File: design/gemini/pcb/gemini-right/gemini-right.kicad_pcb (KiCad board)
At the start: 2 copper layers, 123.8 x 84.2 mm, 47 parts, among them J1 USB-C link, SW00 Y, SW01 U, SW02 I, SW03 O, SW04 P, SW05 Bksp, SW10 H, SW11 J, SW12 K, SW13 L, SW14 ;, SW15 Enter, SW20 N, SW21 M, SW22 ,, SW23 ., SW24 Shift, SW30 Space, SW31 Fn, SW32 Alt, SW33 Ctrl, U1 MCP23017-E/SO

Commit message: add LEDs
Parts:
- added C2: 1uF, C_0603_1608Metric, B.Cu at (24.0, -4.00)
- added C3: 1uF, C_0603_1608Metric, B.Cu at (36.0, -4.00)
- added LED00: SK6812MINI-E, LED_SK6812MINI-E_3.2x2.8mm_P1.5mm_ReverseMount, B.Cu at (9.53, 14.6)
- added LED01: SK6812MINI-E, LED_SK6812MINI-E_3.2x2.8mm_P1.5mm_ReverseMount, B.Cu at (28.6, 14.6)
- added LED02: SK6812MINI-E, LED_SK6812MINI-E_3.2x2.8mm_P1.5mm_ReverseMount, B.Cu at (47.6, 14.6)
- added LED03: SK6812MINI-E, LED_SK6812MINI-E_3.2x2.8mm_P1.5mm_ReverseMount, B.Cu at (66.7, 14.6)
- added LED04: SK6812MINI-E, LED_SK6812MINI-E_3.2x2.8mm_P1.5mm_ReverseMount, B.Cu at (85.7, 14.6)
- added LED05: SK6812MINI-E, LED_SK6812MINI-E_3.2x2.8mm_P1.5mm_ReverseMount, B.Cu at (109.5, 14.6)
- added LED10: SK6812MINI-E, LED_SK6812MINI-E_3.2x2.8mm_P1.5mm_ReverseMount, B.Cu at (14.3, 33.7)
- added LED11: SK6812MINI-E, LED_SK6812MINI-E_3.2x2.8mm_P1.5mm_ReverseMount, B.Cu at (33.3, 33.7)
- added LED12: SK6812MINI-E, LED_SK6812MINI-E_3.2x2.8mm_P1.5mm_ReverseMount, B.Cu at (52.4, 33.7)
- added LED13: SK6812MINI-E, LED_SK6812MINI-E_3.2x2.8mm_P1.5mm_ReverseMount, B.Cu at (71.4, 33.7)
- added LED14: SK6812MINI-E, LED_SK6812MINI-E_3.2x2.8mm_P1.5mm_ReverseMount, B.Cu at (90.5, 33.7)
- added LED15: SK6812MINI-E, LED_SK6812MINI-E_3.2x2.8mm_P1.5mm_ReverseMount, B.Cu at (111.9, 33.7)
- added LED20: SK6812MINI-E, LED_SK6812MINI-E_3.2x2.8mm_P1.5mm_ReverseMount, B.Cu at (19.1, 52.7)
- added LED21: SK6812MINI-E, LED_SK6812MINI-E_3.2x2.8mm_P1.5mm_ReverseMount, B.Cu at (38.1, 52.7)
- added LED22: SK6812MINI-E, LED_SK6812MINI-E_3.2x2.8mm_P1.5mm_ReverseMount, B.Cu at (57.1, 52.7)
- added LED23: SK6812MINI-E, LED_SK6812MINI-E_3.2x2.8mm_P1.5mm_ReverseMount, B.Cu at (76.2, 52.7)
- added LED24: SK6812MINI-E, LED_SK6812MINI-E_3.2x2.8mm_P1.5mm_ReverseMount, B.Cu at (104.8, 52.7)
- added LED30: SK6812MINI-E, LED_SK6812MINI-E_3.2x2.8mm_P1.5mm_ReverseMount, B.Cu at (26.2, 71.8)
- added LED31: SK6812MINI-E, LED_SK6812MINI-E_3.2x2.8mm_P1.5mm_ReverseMount, B.Cu at (64.3, 71.8)
- added LED32: SK6812MINI-E, LED_SK6812MINI-E_3.2x2.8mm_P1.5mm_ReverseMount, B.Cu at (88.1, 71.8)
- added LED33: SK6812MINI-E, LED_SK6812MINI-E_3.2x2.8mm_P1.5mm_ReverseMount, B.Cu at (111.9, 71.8)
- added U2: MCP1700-3302, SOT-23, B.Cu at (30.0, -4.00)
- moved D10 0.60 mm to (10.3, 36.6)
- moved D11 0.60 mm to (29.3, 36.6)
- moved D12 0.60 mm to (48.4, 36.6)
- moved D13 0.60 mm to (67.4, 36.6)
- moved D14 0.60 mm to (86.5, 36.6)
- moved D15 0.60 mm to (107.9, 36.6)
- moved D20 0.60 mm to (15.1, 55.6)
- moved D21 0.60 mm to (34.1, 55.6)
- moved D22 0.60 mm to (53.1, 55.6)
- moved D23 0.60 mm to (72.2, 55.6)
- moved D24 0.60 mm to (100.8, 55.6)
- moved D00 0.60 mm to (5.53, 17.5)
- moved D01 0.60 mm to (24.6, 17.5)
- moved D02 0.60 mm to (43.6, 17.5)
- moved D03 0.60 mm to (62.7, 17.5)
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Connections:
- J1 pad 10: (no net) -> LED_LINK
- J1 pad 11: +3V3 -> +5V
- J1 pad 2: +3V3 -> +5V
- J1 pad 3: (no net) -> LED_LINK
- J1 pad 4: (no net) -> LED_LINK
- J1 pad 9: (no net) -> LED_LINK

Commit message: add usb c
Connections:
- net +5V renamed VSYS

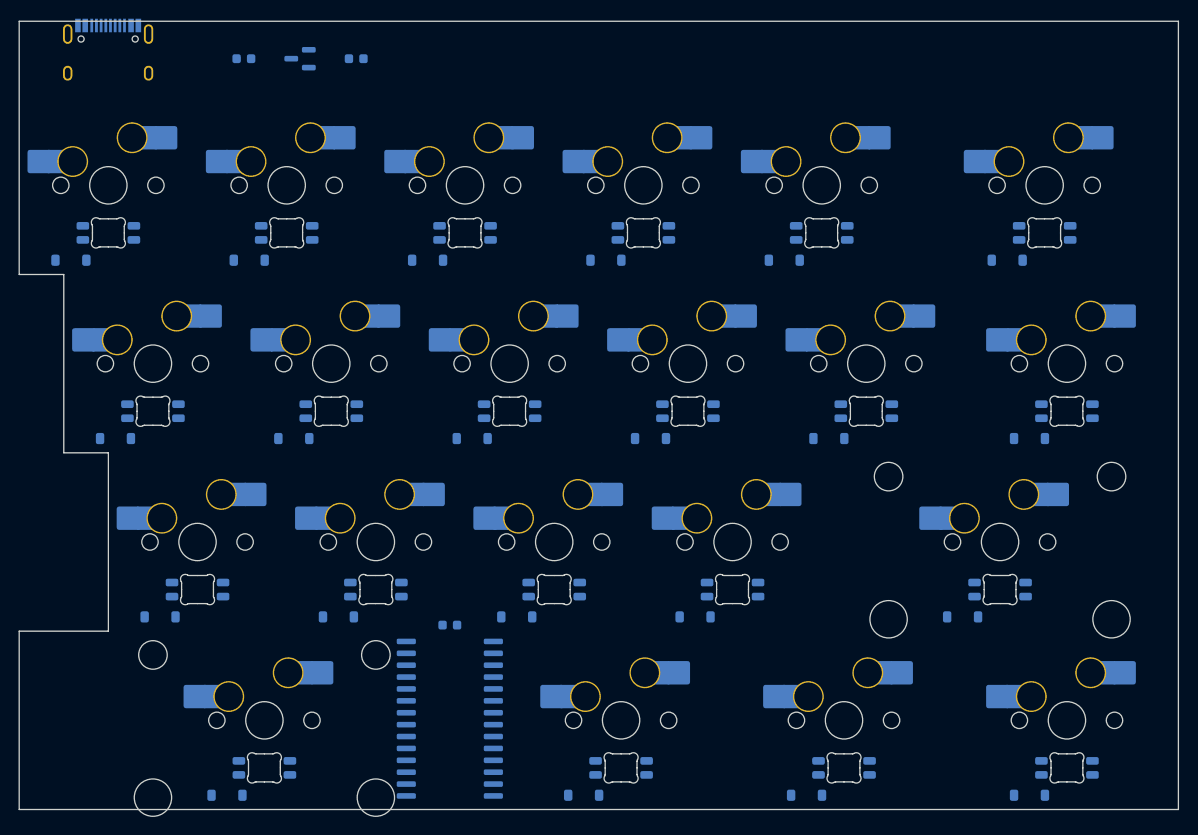
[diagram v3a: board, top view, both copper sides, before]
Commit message: add frontplate browline cover, add joining wall edges
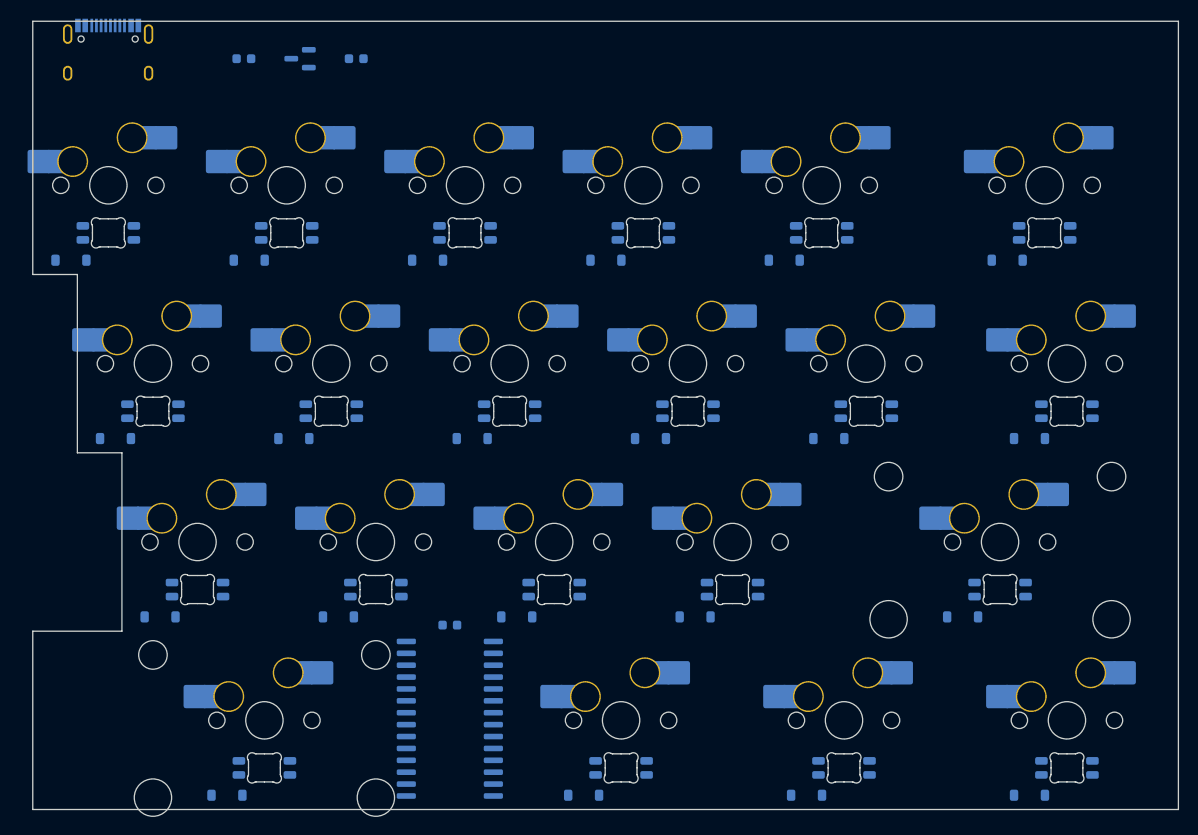
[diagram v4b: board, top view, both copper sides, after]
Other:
- board size 123.8 x 84.2 mm -> 122.4 x 84.2 mm

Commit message: a bunch of fixes
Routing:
- net GND: track 0.00 -> 643.3 mm, vias 0 -> 17
- net VSYS: track 0.00 -> 532.5 mm, vias 0 -> 15
- net COL4: track 0.00 -> 168.1 mm, vias 0 -> 2
- net ROW0: track 0.00 -> 162.1 mm, vias 0 -> 4
- net ROW1: track 0.00 -> 154.8 mm, vias 0 -> 3
- net COL3: track 0.00 -> 148.7 mm, vias 0 -> 1
- net SCL: track 0.00 -> 147.7 mm, vias 0 -> 7
- net LED_CH06: track 0.00 -> 131.3 mm, vias 0 -> 2
- net COL2: track 0.00 -> 128.3 mm, vias 0 -> 2
- net COL0: track 0.00 -> 125.4 mm, vias 0 -> 2
- net COL1: track 0.00 -> 123.3 mm
- net COL5: track 0.00 -> 119.2 mm, vias 0 -> 1
- net LED_CH12: track 0.00 -> 115.9 mm, vias 0 -> 2
- net LED_CH17: track 0.00 -> 112.4 mm, vias 0 -> 6
- net ROW3: track 0.00 -> 107.7 mm, vias 0 -> 5
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- added copper zone on B.Cu, net GND
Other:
- board size 122.4 x 84.2 mm -> 123.1 x 84.2 mm

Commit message: add silkscreening, and layer visibility for model view
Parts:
- added G1: Logo_Gemini, Logo_Gemini, F.Cu at (62.3, -4.00)
